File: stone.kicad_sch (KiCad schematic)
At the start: 43 parts, among them J1 Conn_ARM_SWD_TagConnect_TC203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, J2 UHF_ANT, J3 GNSS_ANT, Q1 AO3400A, Q4 DMC2710UV-7, U1 STM32C011F4Ux, U2 LIS2DH, U3 LP5912-3.3DRV, U4 MAX-M10S, U5 E22-400MM22S

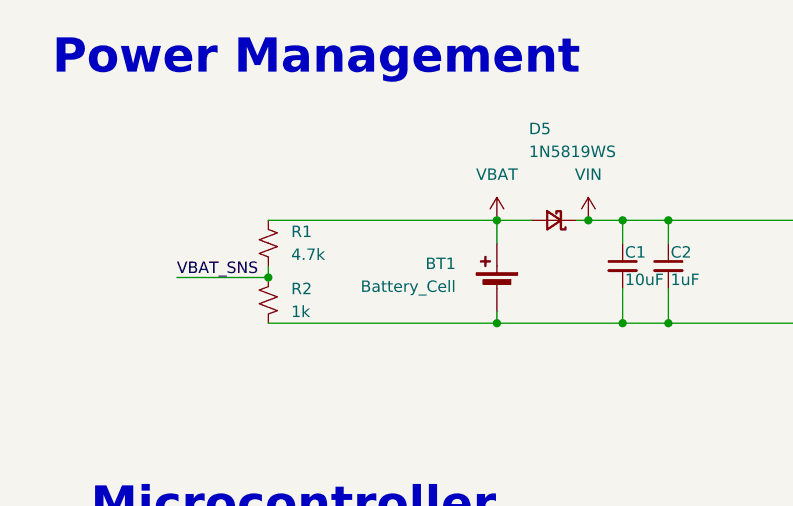
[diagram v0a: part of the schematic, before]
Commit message: added reverse voltage p fet
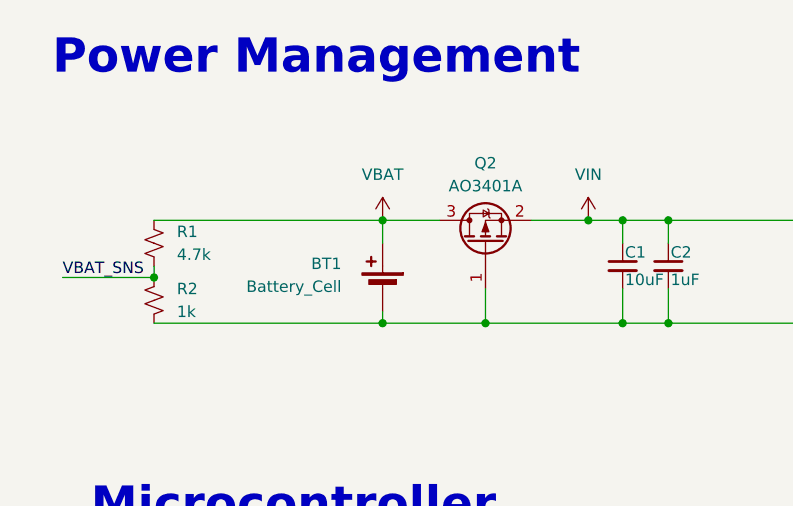
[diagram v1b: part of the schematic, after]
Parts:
- removed D5: 1N5819WS, Diode_SMD:D_SOD-323, symbol Avionics_Symbols:1N5819WS
- added Q2: AO3401A, Package_TO_SOT_SMD:SOT-23, symbol Transistor_FET:AO3401A
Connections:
- net GND: now also Q2.1 (G)
- net VBAT: now also Q2.3 (D)
- net VIN: now also Q2.2 (S)
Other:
- moved on the sheet: BT1, R1, R2
